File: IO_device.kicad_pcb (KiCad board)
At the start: 4 copper layers, 274 parts, among them J1 Screw_Terminal_01x02, J10 Screw_Terminal_01x02, J11 Screw_Terminal_01x02, J12 Screw_Terminal_01x02, J13 USB_C_Receptacle_PowerOnly_6P, J14 Conn_01x01, J15 Screw_Terminal_01x03, J17 Conn_01x01, J18 Conn_01x01, J19 Conn_01x01, J2 Screw_Terminal_01x02, J3 Screw_Terminal_01x02, J4 Screw_Terminal_01x02, J5 Screw_Terminal_01x02, J6 Screw_Terminal_01x02, J7 Screw_Terminal_01x02, J8 Screw_Terminal_01x02, J9 Screw_Terminal_01x02, K1 SDT-S-103DMR,000, K2 SDT-S-103DMR,000, K3 SDT-S-103DMR,000, K4 SDT-S-103DMR,000, Q1 BC847, Q11 BC847, Q12 BC847, Q13 AO3400A, Q2 BC847, Q3 BC847, Q4 BC847, Q5 2SCR587D3, Q6 2SCR587D3, Q7 AO3400A, Q8 AO3400A, Q9 AO3400A, U1 MCP4728, U10 74HC240D, U11 TL071, U12 TL071, U13 IL300-DEFG-X007T, U14 IL300-DEFG-X007T, U15 TL071, U16 TL071, U17 MCP3208T-BI/SL, U18 CNY173SR2VM, U19 CNY173SR2VM, U2 TL071, U20 CNY173SR2VM, U21 CNY173SR2VM, U22 MM74HC14M, U24 TBA1-0522E, U25 TBA1-0522E, U26 TBA1-0522E, U27 ADM2483xRW, U28 NUCLEO-L152RE, U3 TL071, U4 IL300-DEFG-X007T, U5 IL300-DEFG-X007T, U6 TL071, U7 TL071, U8 TL071, U9 TL071

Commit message: alueet laatikoitu, ensimmäiset input osat laitettu
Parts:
- C1, C10, C11, C12, C13, C14, C15, C16, C17, C18, C19, C2, C20, C21, C22, C23, C24, C25, C26, C27, C28, C29, C3, C30, C31, C32, C33, C34, C35, C36, C37, C38, C39, C4, C40, C41, C42, C43, C44, C45, C46, C47, C48, C49, C5, C50, C51, C52, C53, C54, C55, C56, C57, C58, C59, C6, C60, C61, C62, C63, C64, C65, C66, C67, C68, C69, C7, C70, C71, C72, C73, C74, C75, C76, C77, C78, C79, C8, C80, C81, C9, D1, D10, D11, D12, D13, D14, D15, D16, D17, D18, D19, D2, D20, D21, D22, D23, D24, D25, D26, D3, D4, D5, D6, D7, D8, D9, FL1, FL2, J13, J15, K1, K2, K3, K4, L1, L2, L3, L4, L5, L6, PS1, Q1, Q11, Q12, Q13, Q2, Q3, Q4, Q5, Q6, Q7, Q8, Q9, R1, R10, R11, R12, R13, R14, R15, R16, R17, R18, R19, R2, R20, R21, R22, R23, R24, R25, R26, R27, R28, R29, R3, R30, R31, R32, R33, R34, R35, R36, R37, R38, R39, R4, R40, R41, R42, R43, R44, R45, R46, R47, R48, R49, R5, R50, R51, R52, R53, R54, R55, R56, R57, R58, R59, R6, R60, R61, R62, R63, R64, R65, R66, R67, R68, R69, R7, R70, R71, R72, R73, R74, R75, R76, R77, R78, R79, R8, R80, R81, R82, R83, R84, R85, R9, RV1, RV10, RV11, RV12, RV2, RV7, RV8, RV9, U1, U10, U11, U12, U13, U14, U15, U16, U17, U18, U19, U2, U20, U21, U22, U24, U25, U26, U27, U3, U4, U5, U6, U7, U8, U9: moved to B.Cu
- moved J12 372.6 mm to (58.1, 57.4), turned to 90 degrees
- moved J11 362.3 mm to (57.9, 69.1), turned to 90 degrees
- moved J8 357.6 mm to (57.9, 114.5), turned to 90 degrees
- moved RV9 353.0 mm to (66.4, 86.4), turned to -90 degrees
- moved J10 352.3 mm to (57.9, 80.8), turned to 90 degrees
- moved D11 351.9 mm to (84.3, 128.5), turned to -90 degrees
- moved C37 351.7 mm to (87.4, 89.4), turned to -90 degrees
- moved RV10 349.9 mm to (66.4, 73.5), turned to -90 degrees
- moved D12 349.2 mm to (84.8, 110.7), turned to -90 degrees
- moved R70 349.1 mm to (74.7, 68.1), turned to 180 degrees
- moved R69 349.0 mm to (74.7, 61.0), turned to 180 degrees
- moved C38 348.9 mm to (87.4, 76.7), turned to -90 degrees
- moved R71 348.9 mm to (74.7, 48.3), turned to 180 degrees
- moved R72 348.8 mm to (74.7, 55.4), turned to 180 degrees
- moved RV11 347.9 mm to (66.4, 60.8), turned to -90 degrees
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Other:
- board outline added: 160 x 100 mm

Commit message: Janin templaten mukainen
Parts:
- L3, L4, L5, L6, RV1, RV10, RV11, RV12, RV2, RV7, RV8, RV9: moved to F.Cu
- moved U28 311.8 mm to (148.2, 253.5), turned to 90 degrees
- moved K4 285.7 mm to (166.5, 83.1), turned to 0 degrees
- moved K3 282.0 mm to (166.5, 95.6), turned to 0 degrees
- moved K1 281.2 mm to (166.5, 120.7), turned to 0 degrees
- moved K2 280.4 mm to (166.5, 108.2), turned to 0 degrees
- moved C22 269.4 mm to (155.2, 88.4)
- moved C21 267.1 mm to (155.4, 100.7)
- moved C20 265.9 mm to (155.4, 113.5)
- moved C19 265.8 mm to (155.3, 123.1)
- moved C18 262.3 mm to (160.2, 91.0)
- moved C15 261.5 mm to (160.2, 125.9)
- moved C17 261.0 mm to (160.3, 103.2)
- moved C16 260.8 mm to (160.3, 113.5)
- moved R36 246.7 mm to (155.3, 128.7), turned to 0 degrees
- moved R42 242.9 mm to (155.3, 91.0), turned to 0 degrees
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
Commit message: missing AO and power
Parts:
- C75, J13, K1, K2, K3, K4, L1, L2, PS1: moved to F.Cu
- moved C48 338.3 mm to (121.9, 33.5)
- moved C61 337.3 mm to (101.5, 102.1)
- moved C58 331.9 mm to (101.5, 132.0), turned to 0 degrees
- moved C54 331.6 mm to (101.5, 121.9)
- moved C64 327.5 mm to (101.1, 112.3), turned to 0 degrees
- moved C62 323.2 mm to (118.4, 94.3)
- moved C57 315.3 mm to (132.6, 56.4), turned to 90 degrees
- moved C55 314.8 mm to (119.4, 113.6)
- moved C52 310.7 mm to (131.1, 119.1), turned to -90 degrees
- moved C59 307.4 mm to (131.1, 99.9), turned to -90 degrees
- moved C45 305.9 mm to (124.0, 46.2), turned to -90 degrees
- moved C73 293.9 mm to (145.1, 46.2), turned to 90 degrees
- moved PS1 289.1 mm to (130.6, 44.7), turned to 0 degrees
- moved C75 285.5 mm to (153.3, 44.2), turned to 0 degrees
- moved J13 283.2 mm to (138.7, 48.4)
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
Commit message: all components in place
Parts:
- J15, U24, U25, U26: moved to F.Cu
- moved C47 390.5 mm to (62.7, 42.7)
- moved U24 381.7 mm to (76.2, 45.4), turned to -90 degrees
- moved C49 380.6 mm to (75.0, 42.9)
- moved C51 376.5 mm to (66.9, 100.7)
- moved C67 375.6 mm to (55.4, 100.7), turned to 0 degrees
- moved C70 372.5 mm to (60.2, 100.7)
- moved C81 371.6 mm to (67.6, 42.8), turned to 0 degrees
- moved U26 358.1 mm to (68.4, 103.5), turned to -90 degrees
- moved C43 339.7 mm to (113.9, 130.3), turned to 0 degrees
- moved C68 324.5 mm to (118.9, 57.8), turned to 0 degrees
- moved C36 317.1 mm to (135.3, 49.6), turned to 0 degrees
- moved C65 317.0 mm to (123.6, 57.8), turned to 0 degrees
- moved C42 311.8 mm to (135.5, 90.0), turned to 0 degrees
- moved C44 310.8 mm to (141.6, 54.0)
- moved C80 296.9 mm to (136.9, 84.9)
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
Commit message: some of wiring done
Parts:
- moved C1 3.23 mm to (119.4, 70.1)
- moved C65 1.44 mm to (125.1, 57.8)
- moved R9 0.87 mm to (127.1, 65.6), turned to -90 degrees
- moved C68 0.60 mm to (118.3, 57.8)
- moved D2 0.36 mm to (185.3, 48.9)
- moved C44 0.36 mm to (141.6, 54.4)
- moved C13 0.31 mm to (178.0, 48.7)
- moved R28 0.31 mm to (173.3, 48.0)
- moved PS1 0.20 mm to (121.0, 42.9)
- turned C36 to 180 degrees
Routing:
- net DI_1: track 0.00 -> 71.8 mm, vias 0 -> 4
- net Net-(U3--): track 0.00 -> 39.0 mm
- net UART1_RX: track 0.00 -> 36.3 mm
- net Net-(D1-A1): track 0.00 -> 33.9 mm
- net DI_2: track 0.00 -> 32.6 mm, vias 0 -> 2
- net Net-(R77-Pad1): track 0.00 -> 32.5 mm
- net GND3: track 0.00 -> 30.5 mm
- net Net-(U2--): track 0.00 -> 25.8 mm
- net DI_3: track 0.00 -> 25.0 mm, vias 0 -> 2
- net Net-(R78-Pad1): track 0.00 -> 24.1 mm
- net Net-(R80-Pad1): track 0.00 -> 23.9 mm, vias 0 -> 2
- net +12VA: track 0.00 -> 23.6 mm
- net DAC_~{LDAC}: track 0.00 -> 22.6 mm
- net Net-(U6-+): track 0.00 -> 19.2 mm
- net Net-(U9--): track 0.00 -> 18.9 mm
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
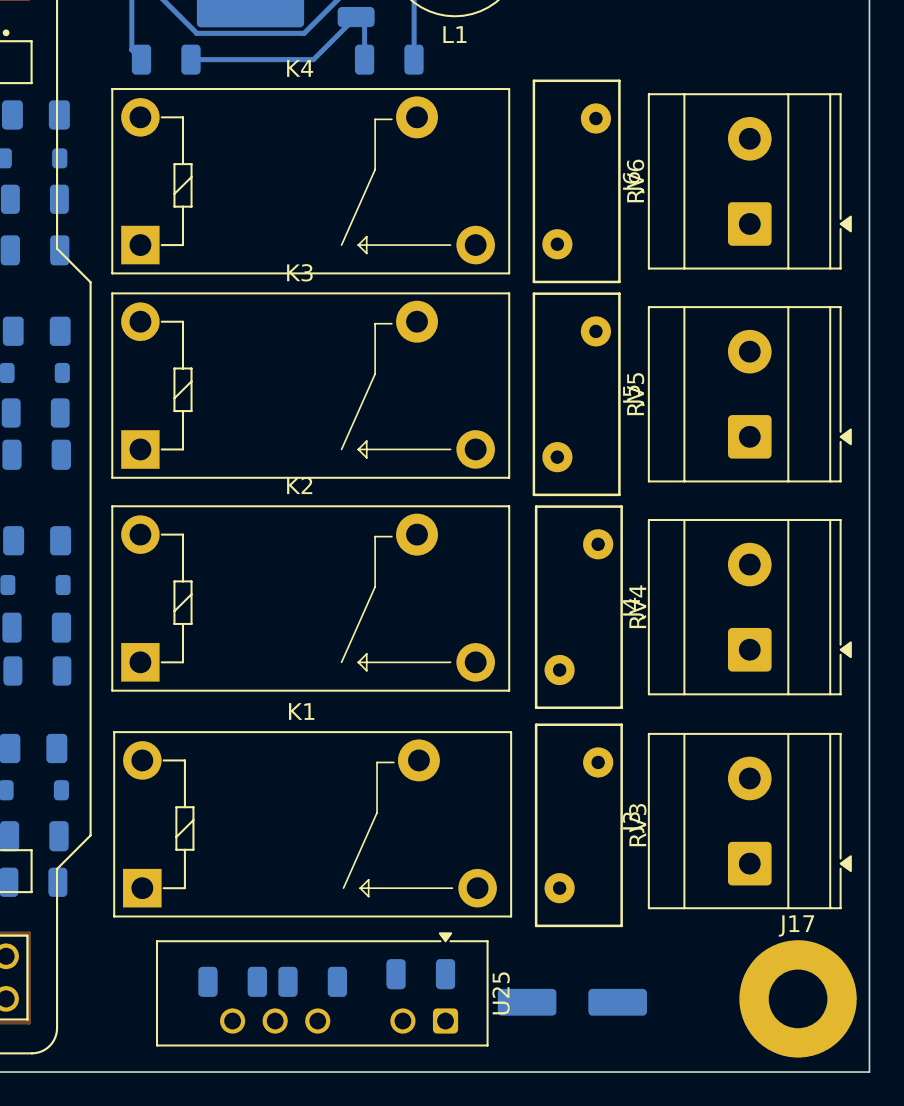
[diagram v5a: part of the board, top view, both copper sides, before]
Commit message: wiring part 2
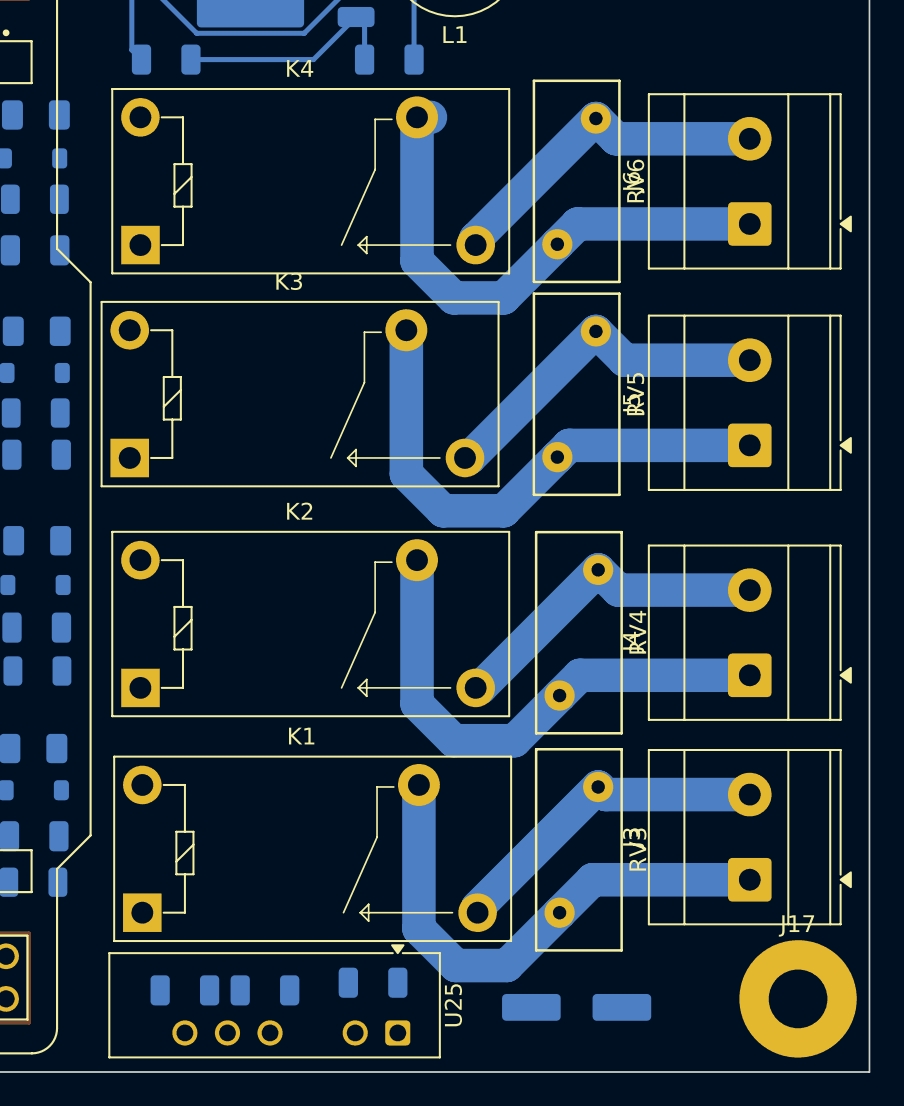
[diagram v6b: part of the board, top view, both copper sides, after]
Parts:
- moved U25 2.93 mm to (181.9, 137.7)
- moved C50 2.89 mm to (180.4, 134.7)
- moved C74 2.89 mm to (169.2, 135.1)
- moved C76 2.89 mm to (173.9, 135.1)
- moved K2 1.52 mm to (166.5, 117.1)
- moved RV4 1.52 mm to (191.5, 117.5)
- moved J4 1.52 mm to (202.9, 116.3)
- moved K1 1.46 mm to (166.6, 130.5)
- moved RV3 1.46 mm to (191.5, 130.5)
- moved J3 0.96 mm to (202.9, 128.5)
- moved K3 0.81 mm to (165.9, 103.4)
- moved J5 0.51 mm to (202.9, 102.6)
- moved C46 0.40 mm to (192.5, 136.1)
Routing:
- net Net-(J6-Pin_1): track 0.00 -> 32.0 mm
- net Net-(J5-Pin_1): track 0.00 -> 31.6 mm
- net Net-(J3-Pin_1): track 0.00 -> 31.3 mm
- net Net-(J4-Pin_1): track 0.00 -> 31.0 mm
- net Net-(J5-Pin_2): track 0.00 -> 20.8 mm
- net Net-(J6-Pin_2): track 0.00 -> 20.2 mm
- net Net-(J4-Pin_2): track 0.00 -> 19.8 mm
- net Net-(J3-Pin_2): track 0.00 -> 19.7 mm

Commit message: started wiring
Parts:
- moved C30 13.0 mm to (114.3, 102.6)
- moved R37 2.79 mm to (160.4, 113.3)
- moved R35 2.69 mm to (160.0, 126.0)
- moved C15 2.60 mm to (160.0, 128.5)
- moved C16 2.35 mm to (160.5, 115.8)
- moved U3 1.34 mm to (134.1, 53.7)
- moved R47 0.32 mm to (96.0, 138.2)
- turned C46 to 0 degrees
- turned D3 to 0 degrees
- turned D4 to 0 degrees
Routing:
- net +3.3V: track 2.70 -> 90.0 mm, vias 0 -> 4
- net +12V: track 13.2 -> 90.1 mm, vias 0 -> 8
- net Net-(J15-Pin_2): track 0.00 -> 71.2 mm, vias 0 -> 2
- net Net-(J15-Pin_1): track 0.75 -> 69.6 mm, vias 0 -> 2
- net DO_OE: track 0.00 -> 51.8 mm, vias 0 -> 2
- net DO1: track 0.00 -> 51.2 mm
- net DO_4: track 0.00 -> 47.5 mm
- net DO2: track 0.00 -> 42.2 mm
- net DI_4: track 7.35 -> 48.6 mm, vias 0 -> 2
- net DO_3: track 0.00 -> 39.5 mm
- net DO_2: track 0.00 -> 36.9 mm
- net DO_1: track 0.00 -> 36.5 mm
- net DO3: track 0.00 -> 33.4 mm
- net +12VA: track 23.6 -> 56.7 mm
- net GNDD: track 13.2 -> 46.1 mm
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
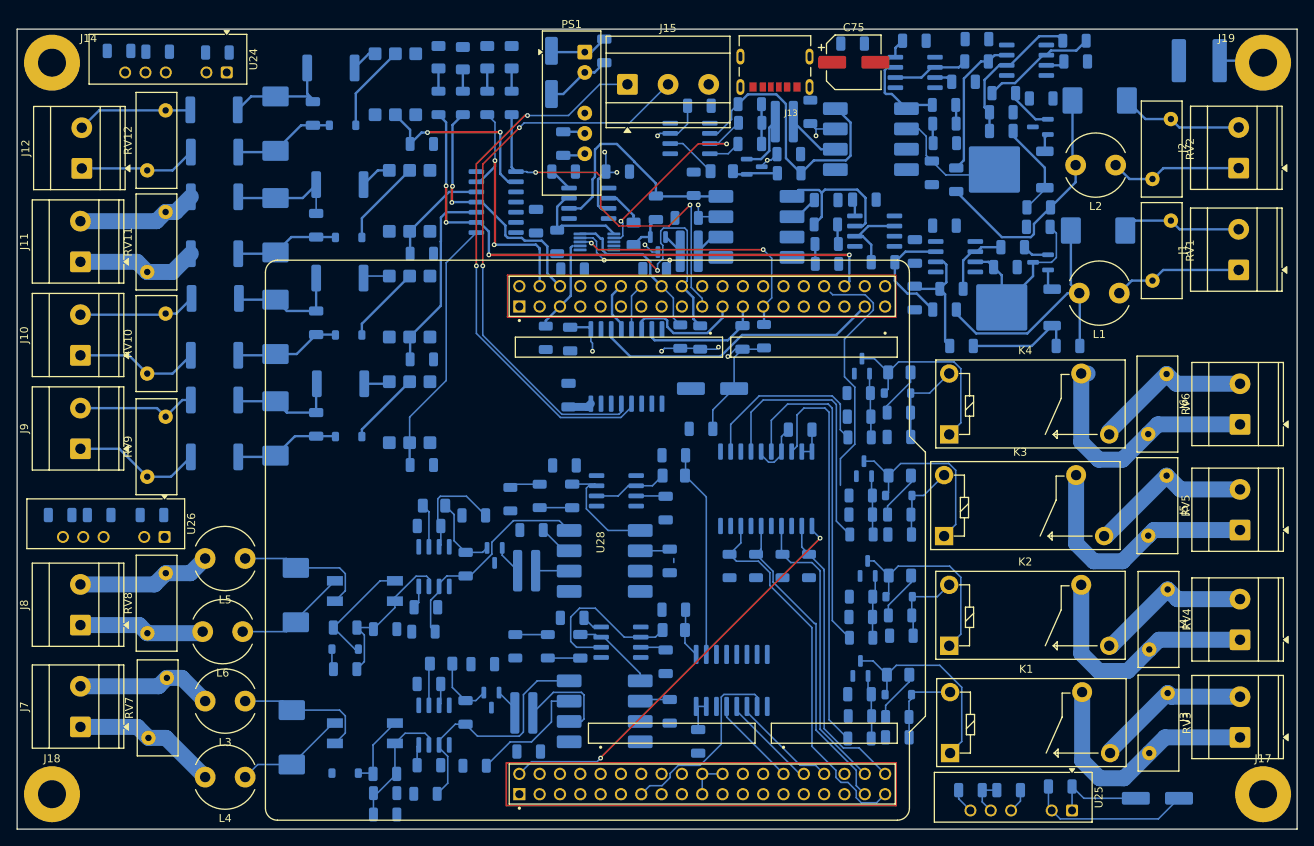
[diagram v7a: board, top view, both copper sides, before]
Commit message: all routed, no errors, missing copper
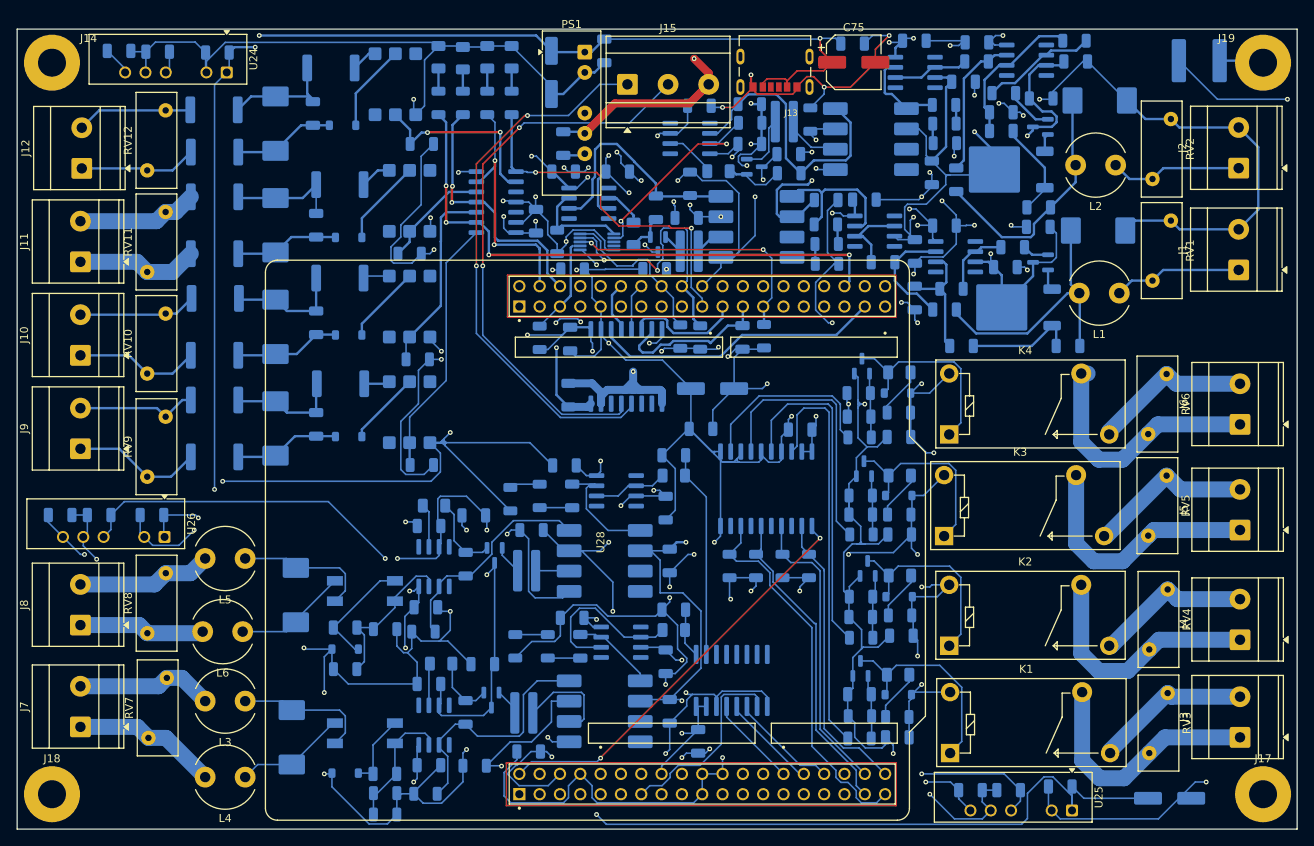
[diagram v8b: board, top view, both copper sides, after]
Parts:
- moved C46 1.52 mm to (194.1, 136.1)
- moved R79 1.52 mm to (99.1, 68.1)
- moved C7 0.97 mm to (149.1, 51.3)
- moved R1 0.76 mm to (115.3, 78.6)
- moved R78 0.51 mm to (100.1, 81.3)
- moved R7 0.46 mm to (134.1, 59.3)
- moved C72 0.41 mm to (170.0, 41.7)
- moved R10 0.41 mm to (137.7, 57.8)
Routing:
- net GNDD: track 46.1 -> 884.7 mm, vias 0 -> 45
- net E5V: track 18.9 -> 394.3 mm, vias 0 -> 11
- net GND3: track 35.3 -> 269.8 mm, vias 0 -> 17
- net +3.3V: track 90.0 -> 323.7 mm, vias 4 -> 22
- net +12VA: track 56.7 -> 280.0 mm, vias 0 -> 8
- net GND2: track 2.58 -> 200.0 mm, vias 0 -> 10
- net +12V: track 90.1 -> 276.2 mm, vias 8 -> 15
- net -12V: track 9.64 -> 164.9 mm, vias 0 -> 5
- net -12VA: track 7.60 -> 151.8 mm, vias 0 -> 7
- net GND: track 2.78 -> 134.8 mm, vias 0 -> 2
- net +12VA2: track 16.1 -> 106.2 mm, vias 0 -> 4
- net -12VA2: track 5.47 -> 78.3 mm, vias 0 -> 4
- net +3.3VA: track 5.74 -> 39.5 mm, vias 0 -> 1
- net (no net): track 32.0 -> 0.00 mm
- net PV: track 15.7 -> 20.2 mm
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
